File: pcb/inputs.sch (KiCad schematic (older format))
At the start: 83 parts, among them P90 5v, P92 GND, P93 MAP, U11 MPXA6115AC6U, U4 MAX9926UAEE+, U6 MPXA4250AC6U

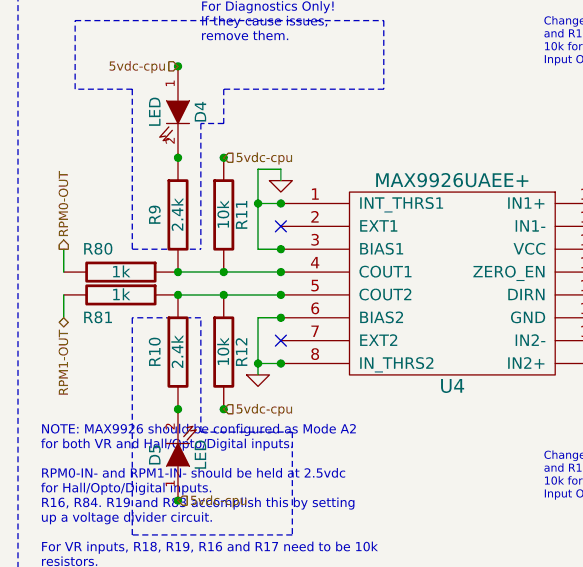
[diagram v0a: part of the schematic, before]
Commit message: Changed 2.4k ohm resistor to 2.43k ohm resistor due to physical size issue.
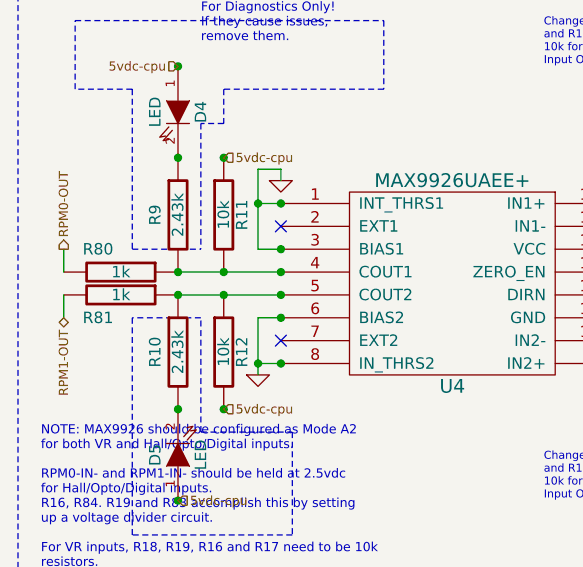
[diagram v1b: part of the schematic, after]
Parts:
- R10, R9: value 2.4k -> 2.43k

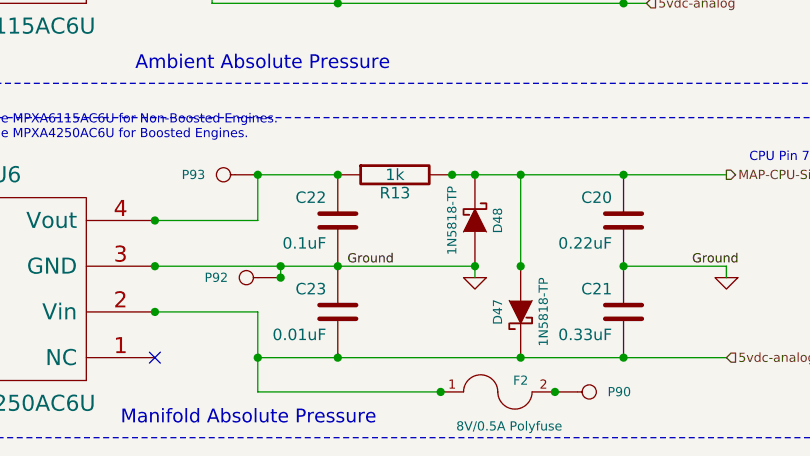
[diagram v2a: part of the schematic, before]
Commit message: Eliminated Pxx designations on the wire connection points and replaced them with the PCB silkscreen designations.
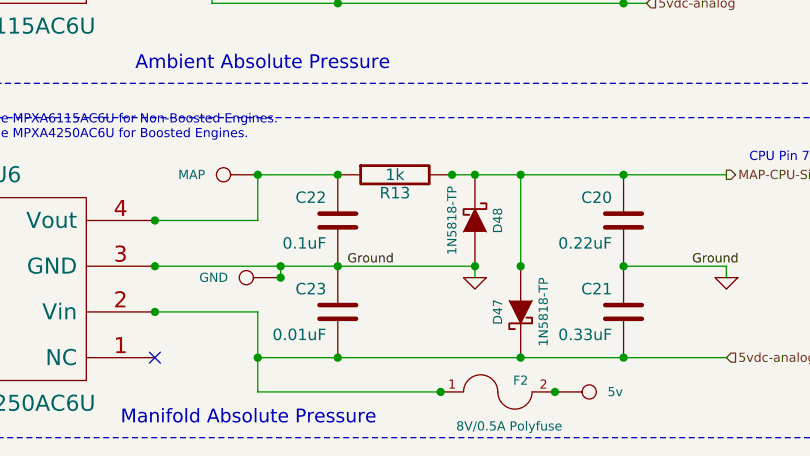
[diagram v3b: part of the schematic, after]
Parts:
- renumbered P90 to 5v, P92 to GND, P93 to MAP
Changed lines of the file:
@@
 Sheet 4 7
 Title "Jaguar PCB for FreeEMS"
-Date "17 nov 2013"
+Date "3 dec 2013"
 Rev "0.6-alpha"
 Comp "Git: 73f4fbd6d6"
@@
 $EndComp
 $Comp
-L CONN_1 P92
+L CONN_1 GND
 U 1 1 509DD6E4
 P 3150 7000
-F 0 "P92" H 3230 7000 40  0000 L CNN
+F 0 "GND" H 3230 7000 40  0000 L CNN
 F 1 "GND" H 3150 7055 30  0001 C CNN
 F 2 "" H 3150 7000 60  0001 C CNN
@@
 $EndComp
 $Comp
-L CONN_1 P90
+L CONN_1 5v
 U 1 1 509DD6DD
 P 4650 7500
-F 0 "P90" H 4730 7500 40  0000 L CNN
+F 0 "5v" H 4730 7500 40  0000 L CNN
 F 1 "5v" H 4650 7555 30  0001 C CNN
 F 2 "" H 4650 7500 60  0001 C CNN
@@
 $EndComp
 $Comp
-L CONN_1 P93
+L CONN_1 MAP
 U 1 1 509DD6C6
 P 3050 6550
-F 0 "P93" H 3130 6550 40  0000 L CNN
+F 0 "MAP" H 3130 6550 40  0000 L CNN
 F 1 "MAP" H 3050 6605 30  0001 C CNN
 F 2 "" H 3050 6550 60  0001 C CNN

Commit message: Added LEDs and resistors to ignitor outputs.
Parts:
- removed F1, F2: 8V/0.5A Polyfuse, symbol FUSE
- added F?: 15V/0.5A Polyfuse, symbol SMD
- R?: renamed from R23; value 5.1k -> 5k
- R?: renamed from R20; value 5.1k -> 5k
- R?: renamed from R9; value 2.43k -> 2.4k
- R?: renamed from R10; value 2.43k -> 2.4k
- renumbered C20 to C?, C21 to C?, C23 to C?, C30 to C?, C28 to C?, C35 to C?, C37 to C?, C29 to C?, C31 to C?, C51 to C?, C36 to C?, C33 to C?, C32 to C?, C27 to C?, C49 to C?, C22 to C?, C26 to C?, C24 to C?, C25 to C?, C42 to C?, C43 to C?, C34 to C?, C38 to C?, C54 to C?, C53 to C?, C56 to C?, C55 to C?, D6 to D?, D7 to D?, D9 to D?, D8 to D?, D15 to D?, D14 to D?, D46 to D?, D45 to D?, D11 to D?, D10 to D?, D13 to D?, D12 to D?, D4 to D?, D5 to D?, D16 to D?, D17 to D?, D47 to D?, D48 to D?, MAP to P?, 5v to P?, GND to P?, R13 to R?, R29 to R?, R30 to R?, R26 to R?, R24 to R?, R34 to R?, R25 to R?, R27 to R?, R82 to R?, R32 to R?, R31 to R?, R28 to R?, R11 to R?, R19 to R?, R18 to R?, R22 to R?, R21 to R?, R16 to R?, R17 to R?, R12 to R?, R80 to R?, R81 to R?, R33 to R?, R84 to R?, R83 to R?, R95 to R?, U4 to U?, U11 to U?, U6 to U?
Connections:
- net labels added: MAT-CPU-Signal, MAT-Sensor
- net labels removed: 5vdc-cpu, SPR-CPU-Signal, SPR-Sensor
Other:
- note added: "For GM DIS and Ford EDIS connect RPM0-IN- and RPM1-IN- to ground.\n\nFor Ford EDIS do not connect RPM1-IN+ to anything either. \nR16, R17, C25, R10, R12 and D5 are not needed for the EDIS system.\n\nR20 and 23 are only to be used with VR Inputs, do not\npopulate these components for GM DIS or Ford EDIS systems."
- note added: "Manifold Air Temperature"
- note added: "This jumper allows us to \njump over Vcc on the PCB"
- note removed: "For GM DIS and Ford EDIS connect RPM0-IN- and RPM1-IN- to ground.\n\nFor Ford EDIS do not connect RPM1-IN+ to anything, it isn't needed\nunless you have a cam sensor for semi-sequential or sequential injection. \nR16, R17, C25, R10, R12 and D5 are not needed for the EDIS system.\n\nR20 and 23 are only to be used with VR Inputs, do not\npopulate these components for GM DIS or Ford EDIS systems."
- note removed: "Spare ADC Input"
- moved on the sheet: P?

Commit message: Changed revision to 0.7-alpha and git hash to xxxxxxxxxx to show that this is in progress.
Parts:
- removed F?: 15V/0.5A Polyfuse, symbol SMD
- added F1, F2: 8V/0.5A Polyfuse, symbol FUSE
- R10, R9: renamed from R?; value 2.4k -> 2.43k
- R20, R23: renamed from R?; value 5k -> 5.1k
- gave numbers to parts that had none: 77
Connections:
- net labels added: 5vdc-cpu, SPR-CPU-Signal, SPR-Sensor
- net labels removed: MAT-CPU-Signal, MAT-Sensor
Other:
- note added: "For GM DIS and Ford EDIS connect RPM0-IN- and RPM1-IN- to ground.\n\nFor Ford EDIS do not connect RPM1-IN+ to anything, it isn't needed\nunless you have a cam sensor for semi-sequential or sequential injection. \nR16, R17, C25, R10, R12 and D5 are not needed for the EDIS system.\n\nR20 and 23 are only to be used with VR Inputs, do not\npopulate these components for GM DIS or Ford EDIS systems."
- note added: "Spare ADC Input"
- note removed: "For GM DIS and Ford EDIS connect RPM0-IN- and RPM1-IN- to ground.\n\nFor Ford EDIS do not connect RPM1-IN+ to anything either. \nR16, R17, C25, R10, R12 and D5 are not needed for the EDIS system.\n\nR20 and 23 are only to be used with VR Inputs, do not\npopulate these components for GM DIS or Ford EDIS systems."
- note removed: "Manifold Air Temperature"
- note removed: "This jumper allows us to \njump over Vcc on the PCB"
- moved on the sheet: 5v

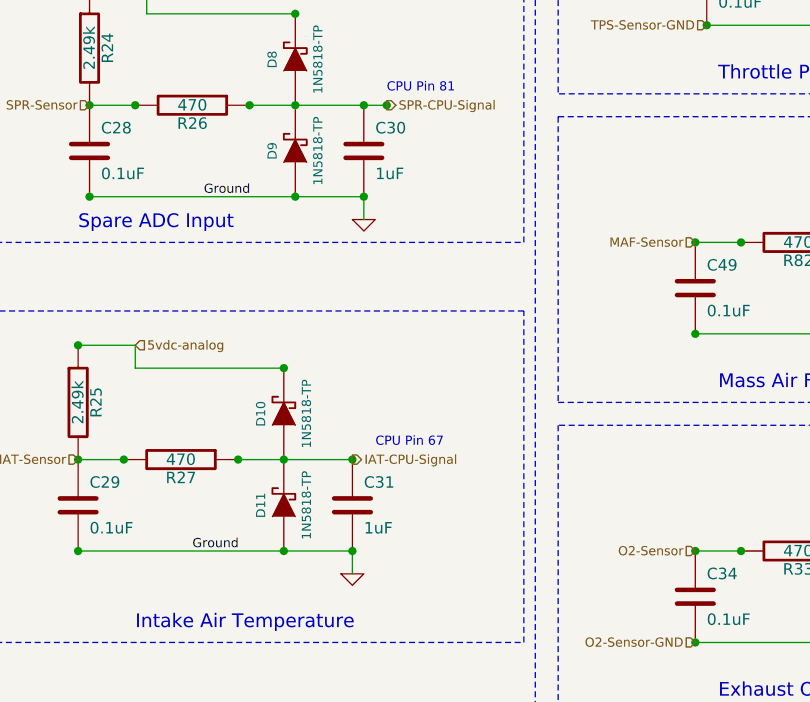
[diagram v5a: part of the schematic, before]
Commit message: Changed Spare ADC and IAT cpu pin capacitor from 1uF to 0.22uF.  Also changed pcb revision to 0.7-alpha.
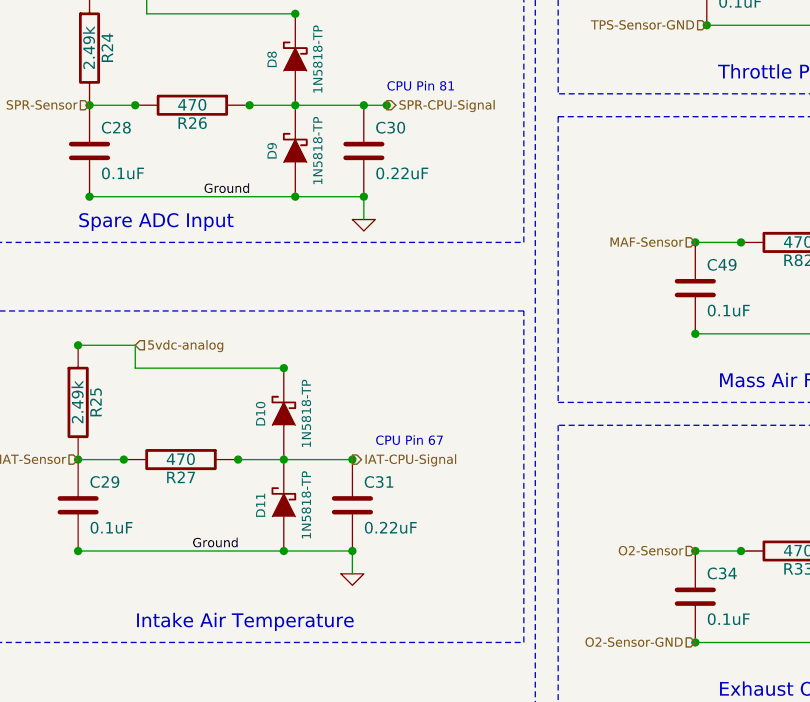
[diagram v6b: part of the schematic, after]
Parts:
- C30, C31: value 1uF -> 0.22uF
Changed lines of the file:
@@
 P 7600 3650
 F 0 "C31" H 7650 3750 50  0000 L CNN
-F 1 "1uF" H 7650 3550 50  0000 L CNN
+F 1 "0.22uF" H 7650 3550 50  0000 L CNN
 F 2 "" H 7600 3650 60  0001 C CNN
 F 3 "" H 7600 3650 60  0001 C CNN
@@
 P 7650 2100
 F 0 "C30" H 7700 2200 50  0000 L CNN
-F 1 "1uF" H 7700 2000 50  0000 L CNN
+F 1 "0.22uF" H 7700 2000 50  0000 L CNN
 F 2 "" H 7650 2100 60  0001 C CNN
 F 3 "" H 7650 2100 60  0001 C CNN

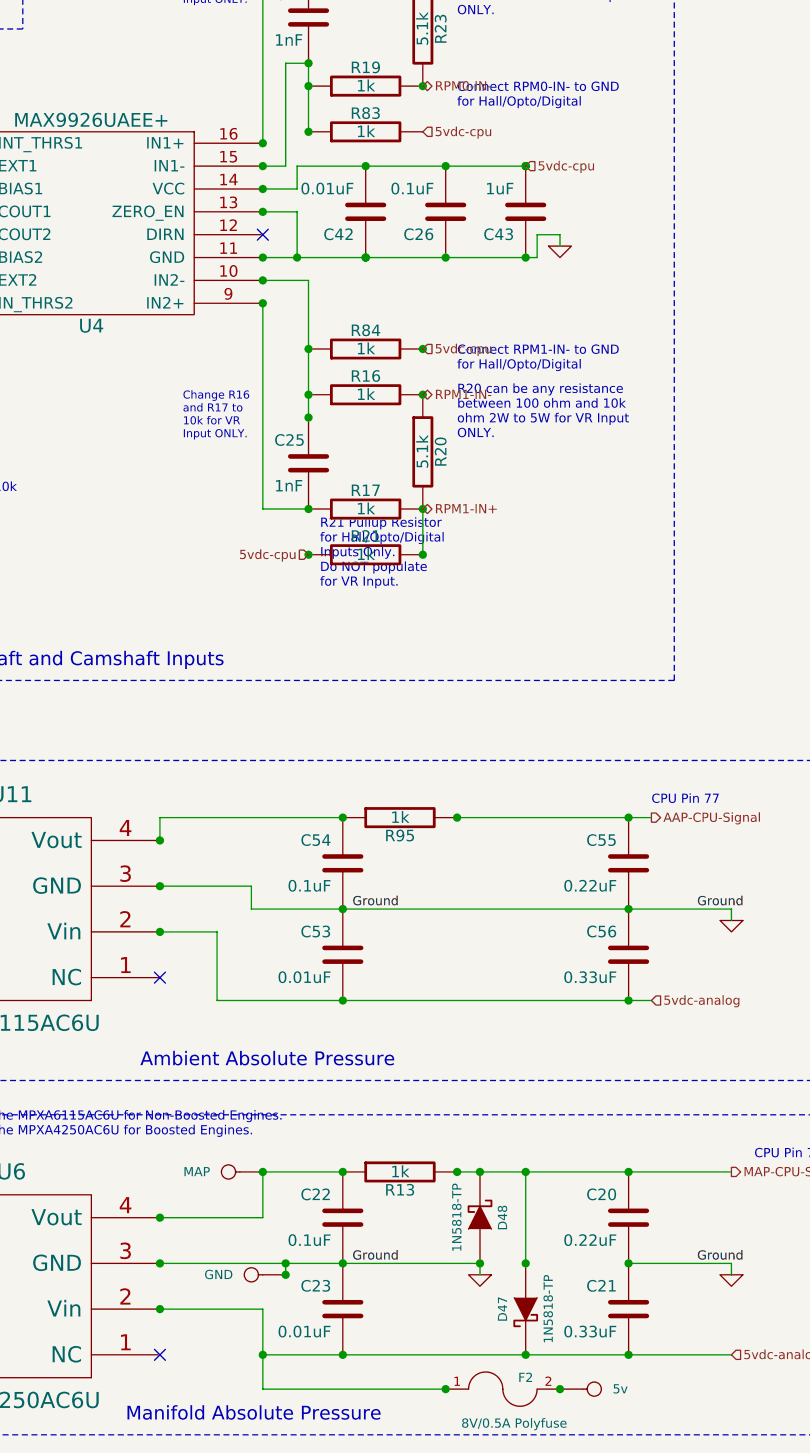
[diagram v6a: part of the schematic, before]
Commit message: Started laying out PCB changes for SO-8 high side driver and new SO-8 low side drivers.
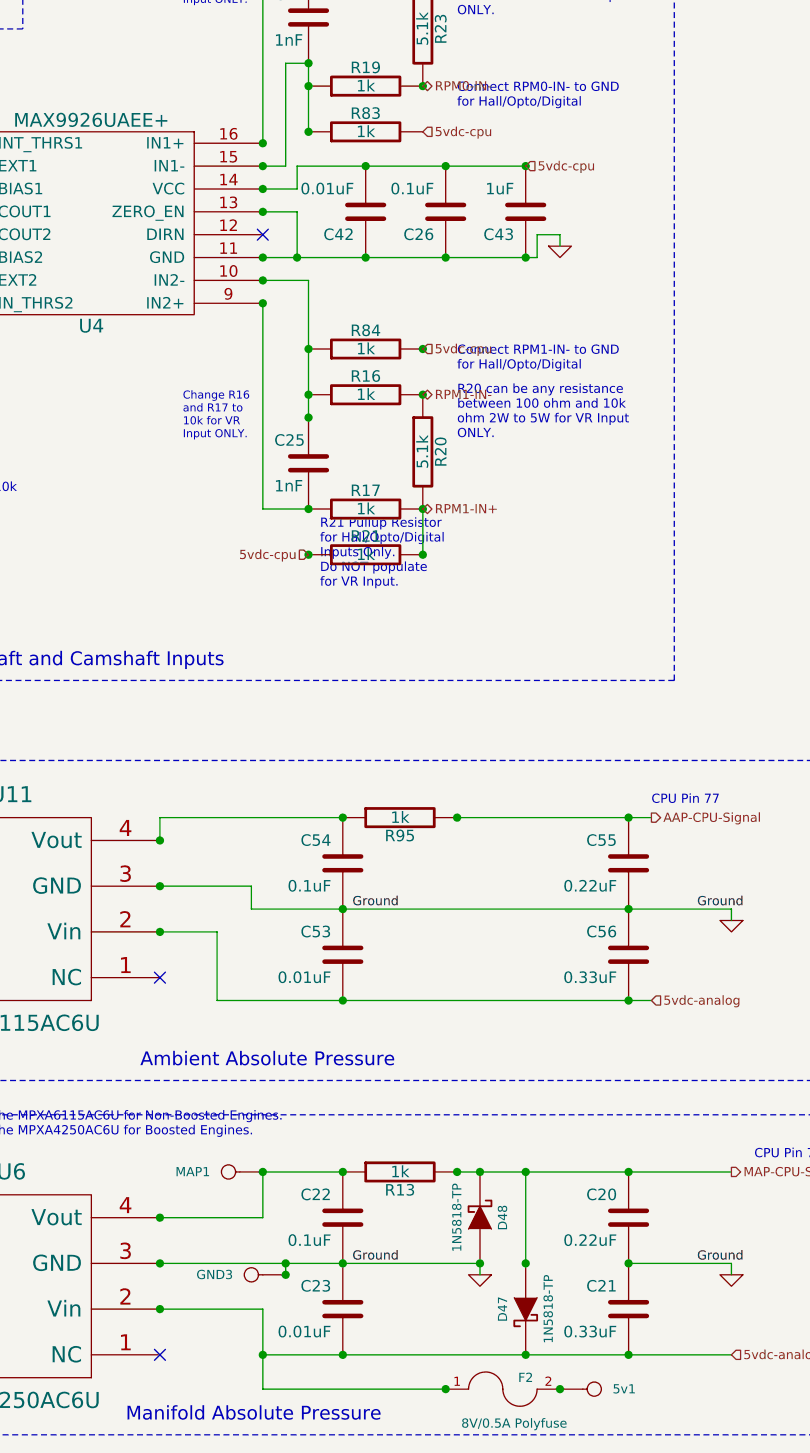
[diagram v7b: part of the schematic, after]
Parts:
- renumbered 5v to 5v1, GND to GND3, MAP to MAP1
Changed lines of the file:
@@
 Sheet 4 7
 Title "Jaguar PCB for FreeEMS"
-Date "5 feb 2014"
+Date "4 mar 2014"
 Rev "0.7-alpha"
 Comp "Git: xxxxxxxxxx"
@@
 Connection ~ 3650 2150
 Connection ~ 4000 2150
-Connection ~ 4350 2150
 Connection ~ 4350 2550
 Connection ~ 4000 2550
-Connection ~ 3650 2550
 Wire Wire Line
 	7650 2300 7650 2400
@@
 $EndComp
 $Comp
-L CONN_1 GND
+L CONN_1 GND3
 U 1 1 509DD6E4
 P 3150 7000
-F 0 "GND" H 3230 7000 40  0000 L CNN
+F 0 "GND3" H 3230 7000 40  0000 L CNN
 F 1 "GND" H 3150 7055 30  0001 C CNN
 F 2 "" H 3150 7000 60  0001 C CNN
@@
 $EndComp
 $Comp
-L CONN_1 5v
+L CONN_1 5v1
 U 1 1 509DD6DD
 P 4650 7500
-F 0 "5v" H 4730 7500 40  0000 L CNN
+F 0 "5v1" H 4730 7500 40  0000 L CNN
 F 1 "5v" H 4650 7555 30  0001 C CNN
 F 2 "" H 4650 7500 60  0001 C CNN
@@
 $EndComp
 $Comp
-L CONN_1 MAP
+L CONN_1 MAP1
 U 1 1 509DD6C6
 P 3050 6550
-F 0 "MAP" H 3130 6550 40  0000 L CNN
+F 0 "MAP1" H 3130 6550 40  0000 L CNN
 F 1 "MAP" H 3050 6605 30  0001 C CNN
 F 2 "" H 3050 6550 60  0001 C CNN
@@
 Ground
 $Comp
-L GND #PWR016
+L GND #PWR20
 U 1 1 5092ECC3
 P 5250 5450
-F 0 "#PWR016" H 5250 5450 30  0001 C CNN
+F 0 "#PWR20" H 5250 5450 30  0001 C CNN
 F 1 "GND" H 5250 5380 30  0001 C CNN
 F 2 "" H 5250 5450 60  0001 C CNN
@@
 Ground
 $Comp
-L GND #PWR017
+L GND #PWR21
 U 1 1 50609B5A
 P 5250 7000
-F 0 "#PWR017" H 5250 7000 30  0001 C CNN
+F 0 "#PWR21" H 5250 7000 30  0001 C CNN
 F 1 "GND" H 5250 6930 30  0001 C CNN
 F 2 "" H 5250 7000 60  0001 C CNN
@@
 $EndComp
 $Comp
-L GND #PWR018
+L GND #PWR28
 U 1 1 5023F4F0
 P 10350 4350
-F 0 "#PWR018" H 10350 4350 30  0001 C CNN
+F 0 "#PWR28" H 10350 4350 30  0001 C CNN
 F 1 "GND" H 10350 4280 30  0001 C CNN
 F 2 "" H 10350 4350 60  0001 C CNN
@@
 Connect RPM1-IN- to GND \nfor Hall/Opto/Digital
 $Comp
-L GND #PWR019
+L GND #PWR16
 U 1 1 4F1D8DAC
 P 1600 2800
-F 0 "#PWR019" H 1600 2800 30  0001 C CNN
+F 0 "#PWR16" H 1600 2800 30  0001 C CNN
 F 1 "GND" H 1600 2730 30  0001 C CNN
 F 2 "" H 1600 2800 60  0001 C CNN
@@
 RPM0-IN-
 $Comp
-L GND #PWR020
+L GND #PWR19
 U 1 1 4F1C330A
 P 4500 2500
-F 0 "#PWR020" H 4500 2500 30  0001 C CNN
+F 0 "#PWR19" H 4500 2500 30  0001 C CNN
 F 1 "GND" H 4500 2430 30  0001 C CNN
 F 2 "" H 4500 2500 60  0001 C CNN
@@
 $EndComp
 $Comp
-L GND #PWR021
+L GND #PWR17
 U 1 1 4F1C32B6
 P 1700 1950
-F 0 "#PWR021" H 1700 1950 30  0001 C CNN
+F 0 "#PWR17" H 1700 1950 30  0001 C CNN
 F 1 "GND" H 1700 1880 30  0001 C CNN
 F 2 "" H 1700 1950 60  0001 C CNN
@@
 $EndComp
 $Comp
-L GND #PWR022
+L GND #PWR18
 U 1 1 4F1C300F
 P 4150 7000
-F 0 "#PWR022" H 4150 7000 30  0001 C CNN
+F 0 "#PWR18" H 4150 7000 30  0001 C CNN
 F 1 "GND" H 4150 6930 30  0001 C CNN
 F 2 "" H 4150 7000 60  0001 C CNN
@@
 $EndComp
 $Comp
-L GND #PWR023
+L GND #PWR27
 U 1 1 4F1C2FFA
 P 10350 3000
-F 0 "#PWR023" H 10350 3000 30  0001 C CNN
+F 0 "#PWR27" H 10350 3000 30  0001 C CNN
 F 1 "GND" H 10350 2930 30  0001 C CNN
 F 2 "" H 10350 3000 60  0001 C CNN
@@
 $EndComp
 $Comp
-L GND #PWR024
+L GND #PWR26
 U 1 1 4F1C2FE3
 P 10350 1650
-F 0 "#PWR024" H 10350 1650 30  0001 C CNN
+F 0 "#PWR26" H 10350 1650 30  0001 C CNN
 F 1 "GND" H 10350 1580 30  0001 C CNN
 F 2 "" H 10350 1650 60  0001 C CNN
@@
 $EndComp
 $Comp
-L GND #PWR025
+L GND #PWR25
 U 1 1 4F1C2F74
 P 8850 5900
-F 0 "#PWR025" H 8850 5900 30  0001 C CNN
+F 0 "#PWR25" H 8850 5900 30  0001 C CNN
 F 1 "GND" H 8850 5830 30  0001 C CNN
 F 2 "" H 8850 5900 60  0001 C CNN
@@
 $EndComp
 $Comp
-L GND #PWR026
+L GND #PWR24
 U 1 1 4F1C2F64
 P 7750 5700
-F 0 "#PWR026" H 7750 5700 30  0001 C CNN
+F 0 "#PWR24" H 7750 5700 30  0001 C CNN
 F 1 "GND" H 7750 5630 30  0001 C CNN
 F 2 "" H 7750 5700 60  0001 C CNN
@@
 $EndComp
 $Comp
-L GND #PWR027
+L GND #PWR22
 U 1 1 4F1C2F0A
 P 7600 3950
-F 0 "#PWR027" H 7600 3950 30  0001 C CNN
+F 0 "#PWR22" H 7600 3950 30  0001 C CNN
 F 1 "GND" H 7600 3880 30  0001 C CNN
 F 2 "" H 7600 3950 60  0001 C CNN
@@
 $EndComp
 $Comp
-L GND #PWR028
+L GND #PWR23
 U 1 1 4F1C2EED
 P 7650 2400
-F 0 "#PWR028" H 7650 2400 30  0001 C CNN
+F 0 "#PWR23" H 7650 2400 30  0001 C CNN
 F 1 "GND" H 7650 2330 30  0001 C CNN
 F 2 "" H 7650 2400 60  0001 C CNN
